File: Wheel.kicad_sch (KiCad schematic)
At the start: 4 parts, among them J1 USB_C_Receptacle_USB2.0_16P, U1 STM32F407VGTx

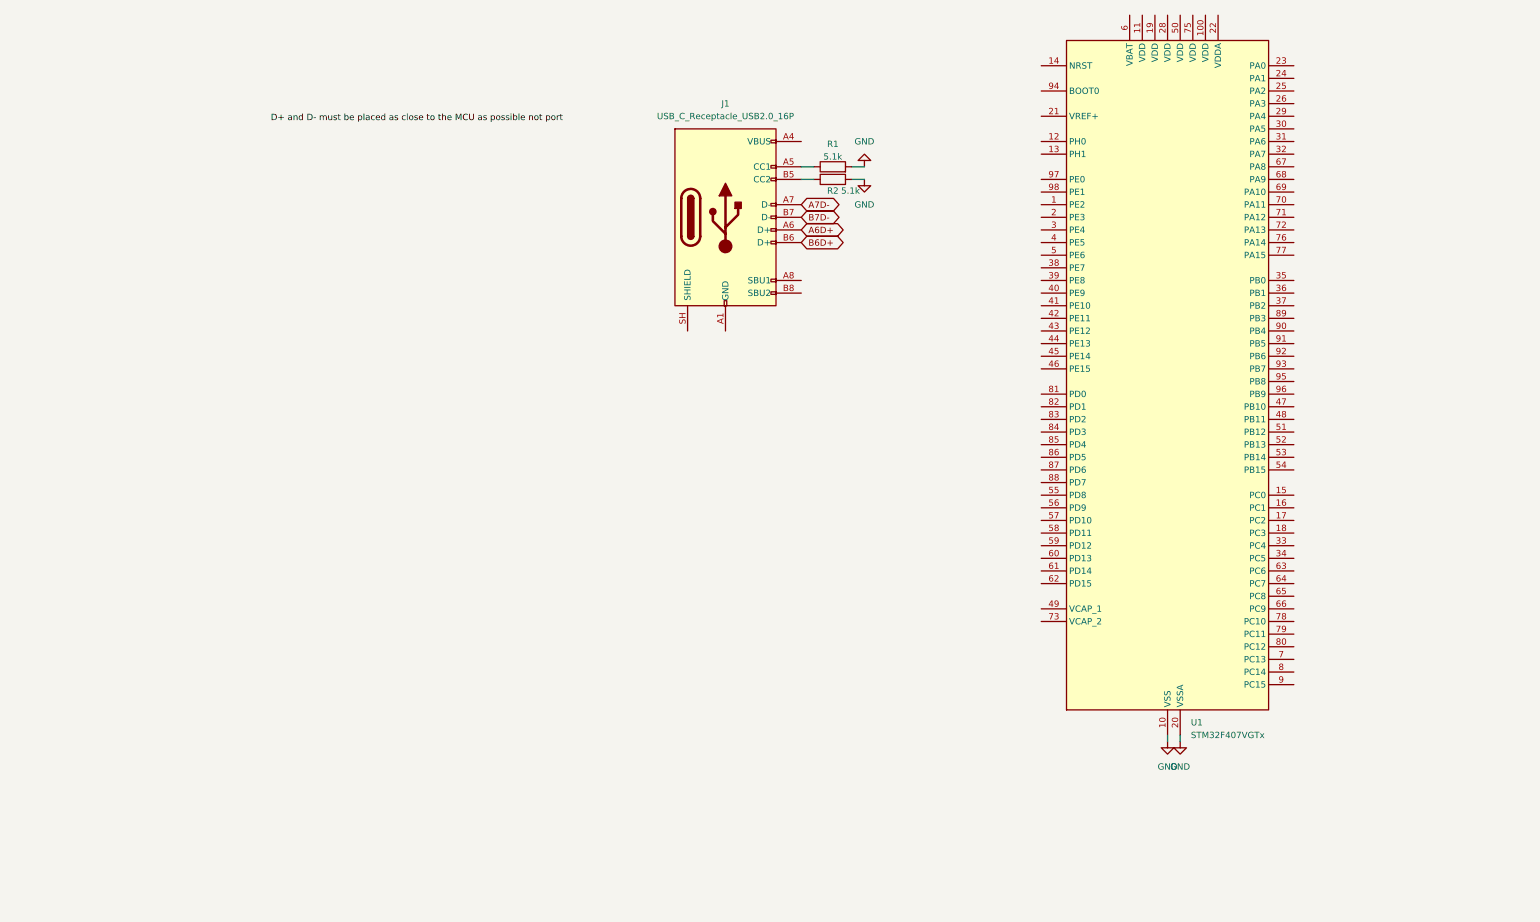
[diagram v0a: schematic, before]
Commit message: Implemented Most of the Schematic
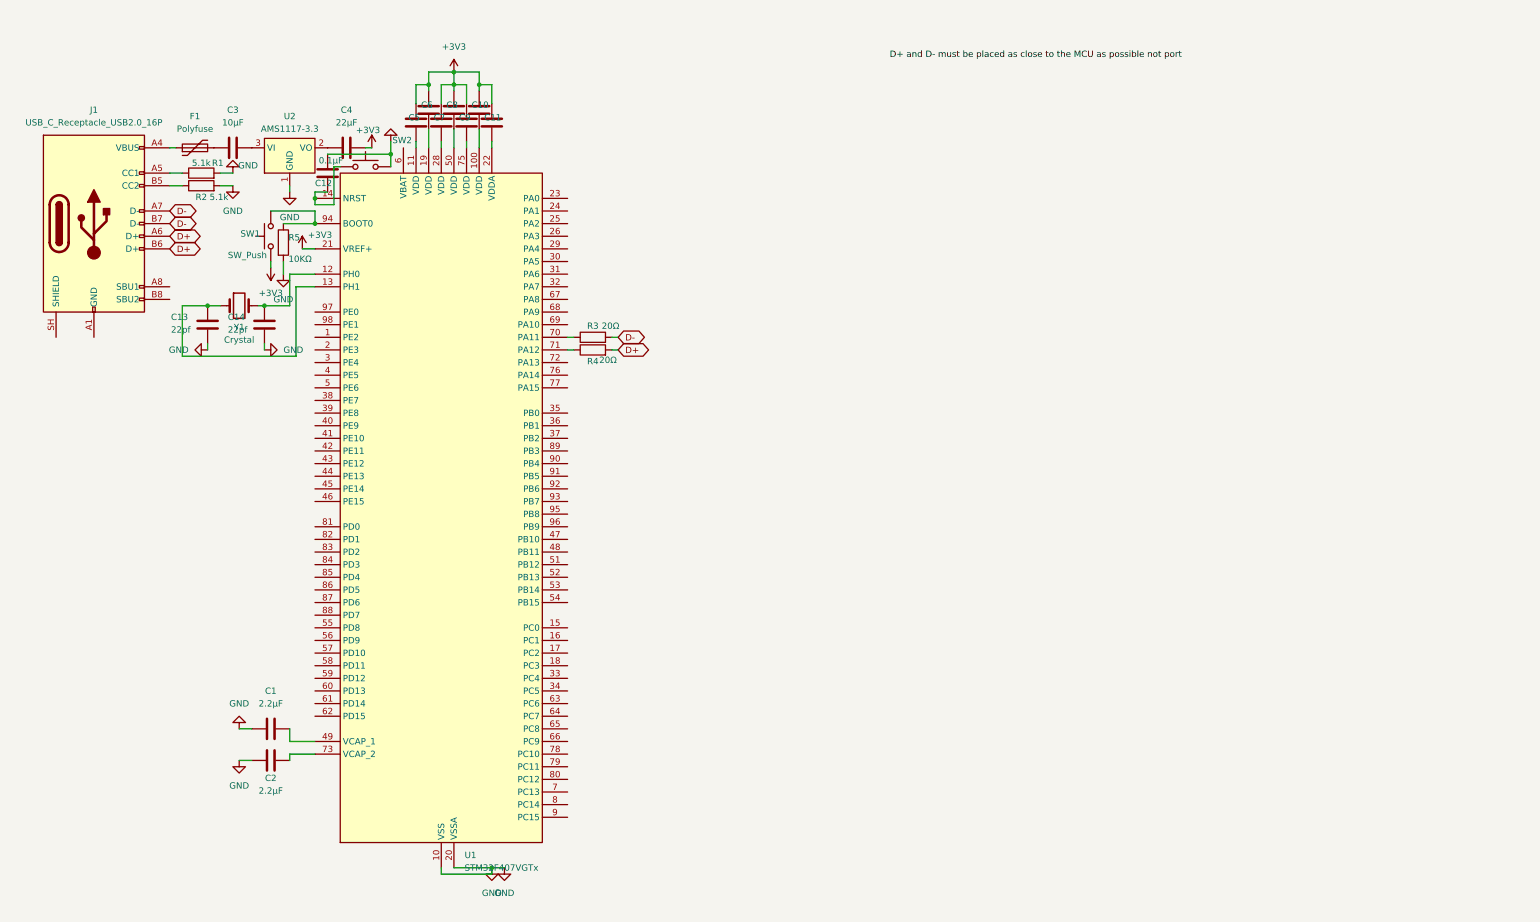
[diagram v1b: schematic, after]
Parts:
- added C1, C2: 2.2µF, symbol Device:C
- added C10, C11, C5, C6, C7, C8, C9: 0.1pf, symbol Device:C
- added C12: 0.1µF, symbol Device:C
- added C13, C14: 22pf, symbol Device:C
- added C3: 10µF, symbol Device:C
- added C4: 22µF, symbol Device:C
- added F1: Polyfuse, symbol Device:Polyfuse
- added R3, R4: 20Ω, symbol Device:R
- added R5: 10KΩ, symbol Device:R
- added SW1, SW2: SW_Push, symbol Switch:SW_Push
- added U2: AMS1117-3.3, Package_TO_SOT_SMD:SOT-223-3_TabPin2, symbol Regulator_Linear:AMS1117-3.3
- added Y1: Crystal, symbol Device:Crystal
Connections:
- net B6D+ is gone; now on net D+: J1.B6 (D+)
- net B7D- is gone; now on net D-: J1.B7 (D-)
- net GND: now also C1.1, C12.1, C13.2, C14.2, C2.1, R5.2, SW2.2, U2.1 (GND)
- net at J1.A4 (VBUS), J1.A9 (VBUS), J1.B4 (VBUS)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: now also F1.1
- net at U1.100 (VDD): now also C10.2
- net at U1.11 (VDD): now also C5.2
- net at U1.12 (PH0): now also C14.1, Y1.2
- net at U1.13 (PH1): now also C13.1, Y1.1
- net at U1.14 (NRST): now also C12.2, SW2.1
- net at U1.19 (VDD): now also C6.2
- net +3V3: now reaches U1.21 (VREF+)
- net +3V3: now also C10.1, C11.1, C4.2, C5.1, C6.1, C7.1, C8.1, C9.1, SW1.1
- net at U1.22 (VDDA): now also C11.2
- net at U1.28 (VDD): now also C7.2
- net at U1.49 (VCAP_1): now also C1.2
- net at U1.50 (VDD): now also C8.2
- net at U1.70 (PA11): now also R3.1
- net at U1.71 (PA12): now also R4.1
- net at U1.73 (VCAP_2): now also C2.2
- net at U1.75 (VDD): now also C9.2
- net at U1.94 (BOOT0): now also R5.1, SW1.2
- net A6D+ renamed D+
- net D+: now also R4.2
- net A7D- renamed D-
- net D-: now also R3.2
- new net: C4.1, U2.2 (VO)
- new net: C3.2, U2.3 (VI)
- new net: C3.1, F1.2
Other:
- moved on the sheet: J1, R1, R2, U1

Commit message: Finished Schematic
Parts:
- added J5: Conn_01x06, symbol Connector_Generic:Conn_01x06
- added J6: Conn_01x03, symbol Connector_Generic:Conn_01x03
- added J7: Conn_01x05, symbol Connector_Generic:Conn_01x05
- added R10, R11, R12, R13, R14: 100Ω, symbol Device:R
- added R15: 10k, symbol Device:R
- added R6, R7, R8, R9: 22Ω, symbol Device:R
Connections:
- net +3V3: now also J5.2 (Pin_2), J7.2 (Pin_2), R15.2
- net GND: now also J5.1 (Pin_1), J6.1 (Pin_1), J7.1 (Pin_1)
- net at U1.25 (PA2): now also R10.1
- net at U1.26 (PA3): now also R11.1
- net LATCH/CS: now reaches U1.51 (PB12)
- net LATCH/CS: now also R12.2
- net SCK(S): now reaches U1.52 (PB13)
- net SCK(S): now also R13.2
- net MISO(S): now reaches U1.53 (PB14)
- net MISO(S): now also R14.2, R15.1
- net CSN: now reaches U1.77 (PA15)
- net CSN: now also R9.2
- net SCK: now reaches U1.78 (PC10)
- net SCK: now also R8.2
- net MISO: now reaches U1.79 (PC11)
- net MISO: now also R6.2
- net MOSI: now reaches U1.80 (PC12)
- net MOSI: now also R7.2
- new net: J5.5 (Pin_5), R8.1
- new net: J5.4 (Pin_4), R7.1
- new net: J5.6 (Pin_6), R9.1
- new net: J7.3 (Pin_3), R12.1
- new net: J7.4 (Pin_4), R13.1
- new net: J7.5 (Pin_5), R14.1
- new net: J5.3 (Pin_3), R6.1
- new net HOV_RX: J6.3 (Pin_3), R11.2
- new net HOV_TX: J6.2 (Pin_2), R10.2
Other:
- added sheet MT6835 (untitled.kicad_sch)

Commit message: Update
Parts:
- removed Y1: Crystal, symbol Device:Crystal
- added 8Mhz1: Crystal_GND24, Crystal:Crystal_SMD_3225-4Pin_3.2x2.5mm, symbol Device:Crystal_GND24
- added C17, C19: 1µF, Capacitor_SMD:C_0402_1005Metric, symbol Device:C
- added C18, C20: 10nF, Capacitor_SMD:C_0402_1005Metric, symbol Device:C
- added C21: 100nF, Capacitor_SMD:C_0402_1005Metric, symbol Device:C
- C1, C12, C2: footprint (none) -> Capacitor_SMD:C_0402_1005Metric
- C10, C5, C6, C7, C8, C9: value 0.1pf -> 100nF; footprint (none) -> Capacitor_SMD:C_0402_1005Metric
- C11: value 0.1pf -> 4.7µF; footprint (none) -> Capacitor_SMD:C_0402_1005Metric
- C13, C14: value 22pf -> 27pf; footprint (none) -> Capacitor_SMD:C_0402_1005Metric
- C3: value 10µF -> 22µF; footprint (none) -> Capacitor_SMD:C_0805_2012Metric
- C4: value 22µF -> 10µF; footprint (none) -> Capacitor_SMD:C_0805_2012Metric
- F1: footprint (none) -> Fuse:Fuse_1812_4532Metric
- J1: footprint (none) -> Connector_USB:USB_C_Receptacle_HRO_TYPE-C-31-M-12
- J5: footprint (none) -> Connector_PinHeader_2.54mm:PinHeader_1x06_P2.54mm_Vertical
- J6: footprint (none) -> Connector_PinHeader_2.54mm:PinHeader_1x03_P2.54mm_Vertical
- J7: footprint (none) -> Connector_PinHeader_2.54mm:PinHeader_1x05_P2.54mm_Vertical
- R1, R10, R11, R12, R13, R14, R15, R2, R3, R4, R5, R6, R7, R8, R9: footprint (none) -> Resistor_SMD:R_0402_1005Metric
- SW1: footprint (none) -> Button_Switch_SMD:SW_Push_1P1T_NO_CK_PTS125Sx85SMTR
- SW2: footprint (none) -> Button_Switch_SMD:SW_SPDT_CK_JS102011SAQN
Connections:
- net +3V3: now also U1.6 (VBAT), C17.1, C18.2, C20.1, C21.2; no longer C10.1, C5.1, C6.1, C7.1, C8.1, C9.1
- net GND: now also C13.1, 8Mhz1.2 (G), 8Mhz1.4 (G), C17.2, C18.1, C21.1; no longer C13.2, C14.2
- net at C11.2: now also C10.1, C5.1, C6.1, C7.1, C8.1, C9.1; no longer U1.22 (VDDA)
- net at C14.1: now also U1.13 (PH1); no longer U1.12 (PH0)
- new net: C19.1, C20.2
- new net: C19.2, U1.22 (VDDA)
- new net: 8Mhz1.1, C14.2
- new net: 8Mhz1.3, C13.2, U1.12 (PH0)
